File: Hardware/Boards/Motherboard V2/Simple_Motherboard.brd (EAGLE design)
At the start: 146.1 x 147.3 mm, 129 parts, among them J1 AVR_SPI_PRG_6PTH, J2 U.FL, U1 WIZ811MJ, U1_MUX 74HC4052D,653, U2 ATMEGA328P_PDIP, U2_MUX 74HC4052D,653, U3_MUX 74HC4052D,653, U4_MUX 74HC4052D,653, U5_MUX 74HC4052D,653, U7_MUX 74HC4052D,653, Y1 16MHz

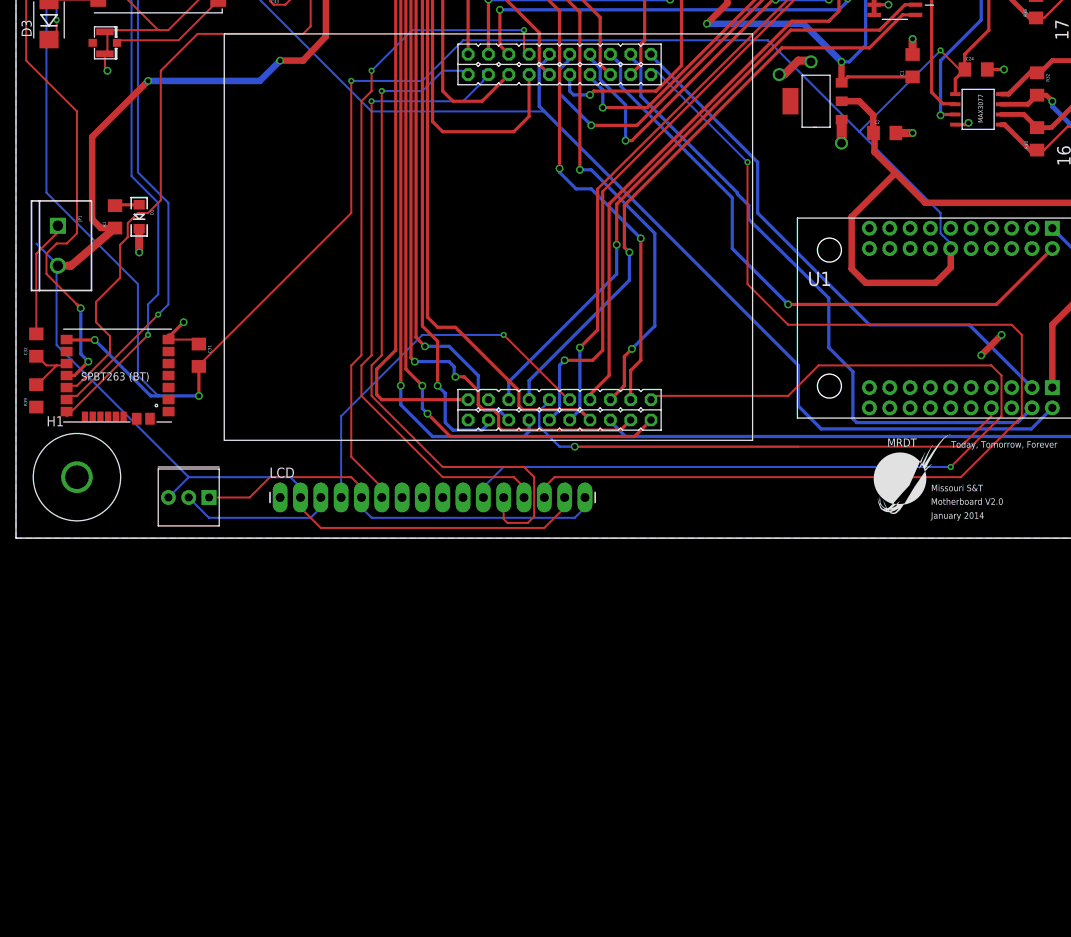
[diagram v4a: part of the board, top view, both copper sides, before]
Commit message: Added fan power connectors, still need to be routed
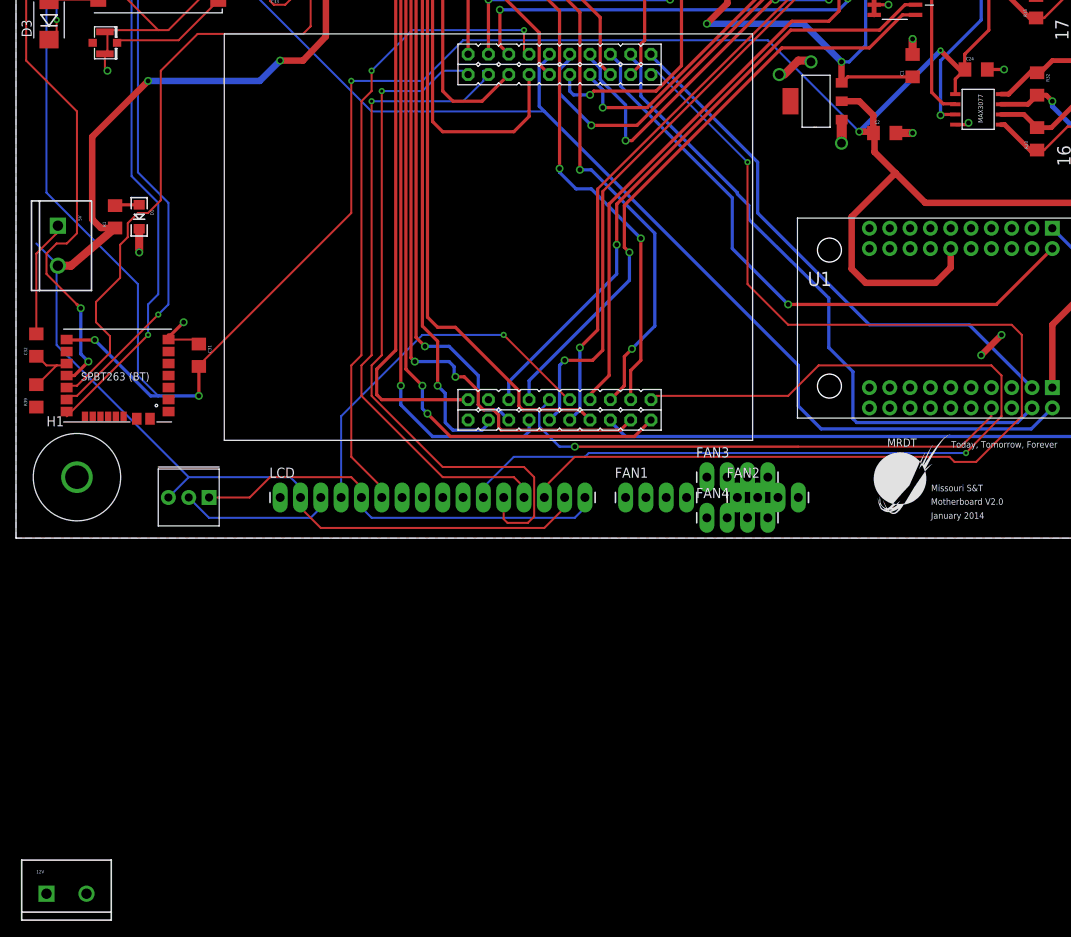
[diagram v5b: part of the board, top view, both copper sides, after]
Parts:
- added 12V: M025MM, SparkFun-Connectors:SCREWTERMINAL-5MM-2
- added FAN1, FAN2, FAN3, FAN4: (no value), SparkFun-Connectors:1X04_LONGPADS
- renumbered JP1 to 5V
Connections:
- new net +12V: 12V.2, FAN1.2, FAN2.2, FAN3.2, FAN4.2
- net GND: now also 12V.1, FAN1.1, FAN2.1, FAN3.1, FAN4.1
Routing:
- net +3V3: track 771.9 -> 755.1 mm, vias 15 -> 16
- net LCD_D7: track 143.9 -> 144.4 mm

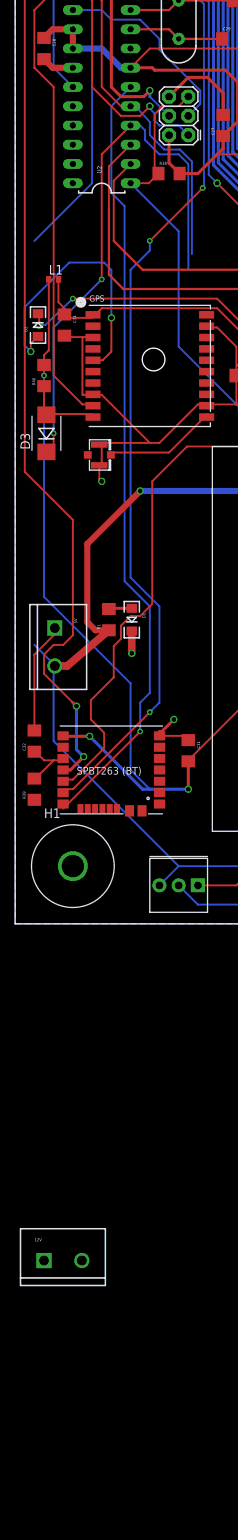
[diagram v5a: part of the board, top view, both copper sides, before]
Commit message: Removed useless traces
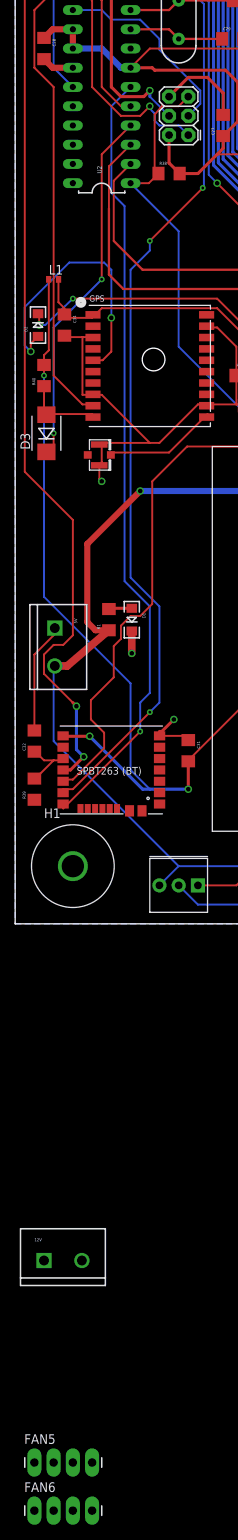
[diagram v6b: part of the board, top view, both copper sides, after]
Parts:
- added FAN5, FAN6: (no value), SparkFun-Connectors:1X04_LONGPADS
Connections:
- net +12V: now also FAN5.2, FAN6.2
- net GND: now also FAN5.1, FAN6.1
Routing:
- net +5V: track 547.3 -> 515.2 mm
- net GPS_RX: track 72.8 -> 48.3 mm
- net GPS_TX: track 108.4 -> 84.0 mm

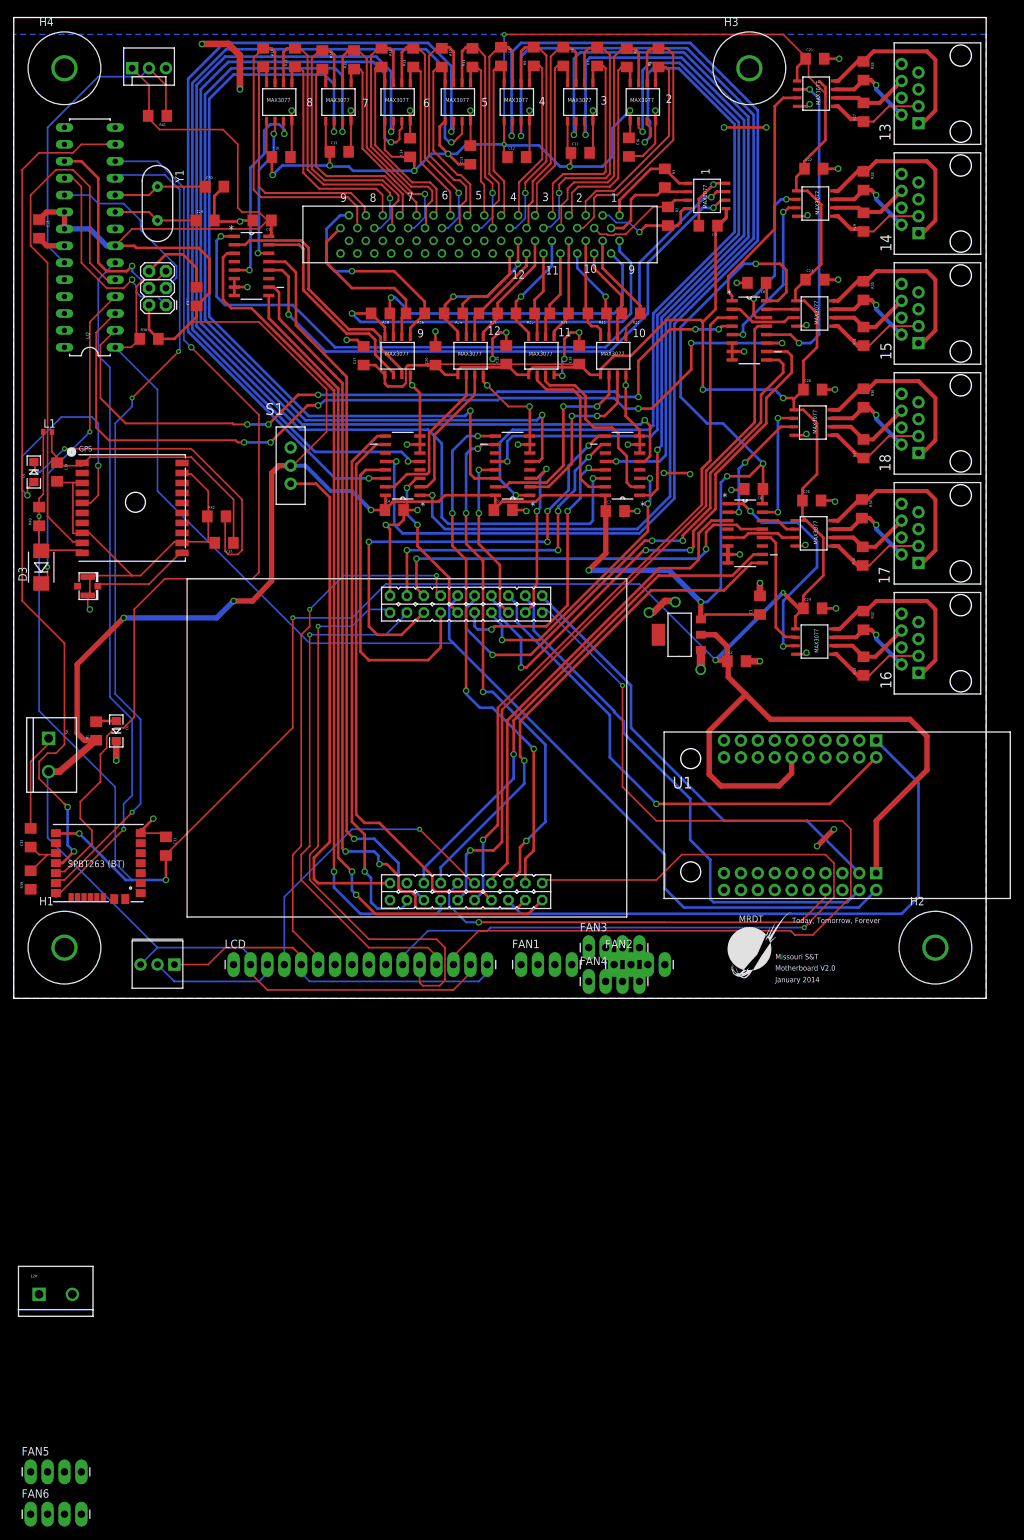
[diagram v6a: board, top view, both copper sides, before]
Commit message: Moved logo to prepare for fan connectors
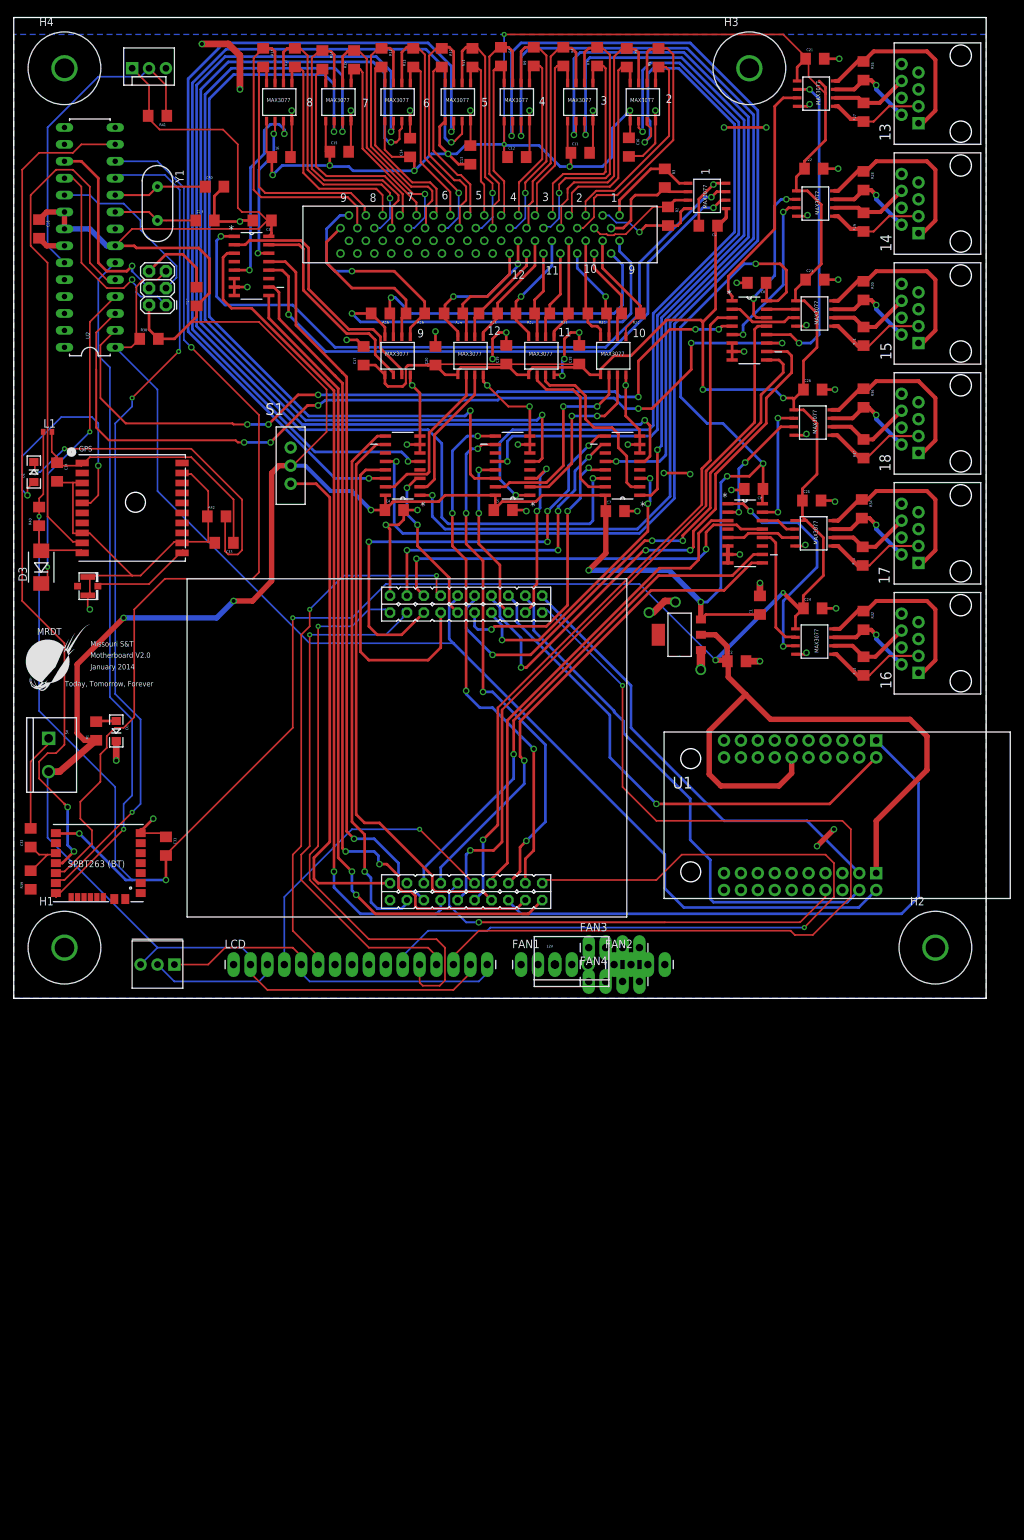
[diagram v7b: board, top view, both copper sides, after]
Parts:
- removed FAN5, FAN6: (no value), SparkFun-Connectors:1X04_LONGPADS
- moved 12V 92.0 mm to (81.3, 5.08)
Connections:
- net +12V: no longer FAN5.2, FAN6.2
- net GND: no longer FAN5.1, FAN6.1

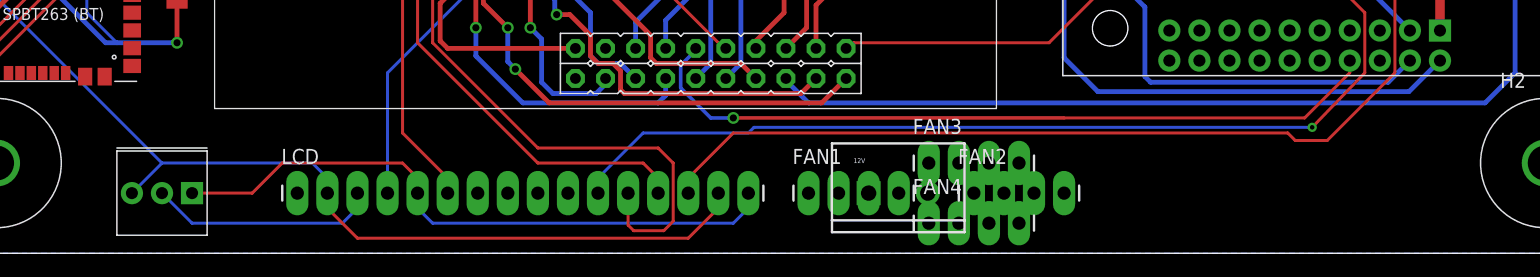
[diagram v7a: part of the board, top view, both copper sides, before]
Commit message: Added fan connectors
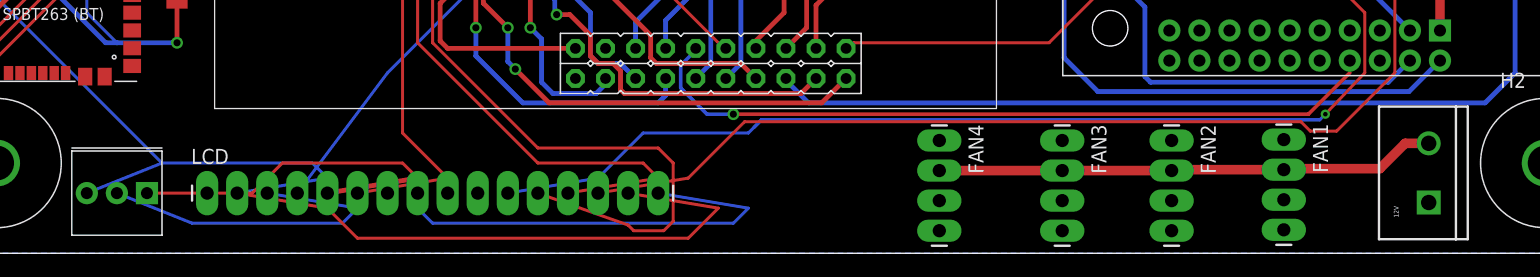
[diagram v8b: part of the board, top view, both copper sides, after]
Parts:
- moved 12V 47.3 mm to (128.6, 4.29), turned to 90 degrees
- moved FAN1 40.4 mm to (116.3, 9.60), turned to 270 degrees
- moved FAN2 17.3 mm to (106.9, 9.53), turned to 270 degrees
- moved FAN3 11.4 mm to (97.6, 9.53), turned to 270 degrees
- moved LCD 7.62 mm to (25.4, 5.08)
- moved FAN4 7.04 mm to (87.2, 9.53), turned to 270 degrees
- moved U$10 3.81 mm to (20.3, 7.62)
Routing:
- net +12V: track 0.00 -> 42.3 mm
- net +5V: track 515.2 -> 537.8 mm
- net GND: track 396.5 -> 413.2 mm
- net N$7: track 19.4 -> 29.1 mm
- net LCD_D7: track 144.4 -> 151.0 mm
- net LCD_D4: track 120.9 -> 127.4 mm
- net LCD_EN: track 80.5 -> 86.9 mm
- net LCD_D6: track 80.8 -> 87.2 mm
- net LCD_D5: track 87.1 -> 92.5 mm
- net LCD_RS: track 46.3 -> 48.8 mm
